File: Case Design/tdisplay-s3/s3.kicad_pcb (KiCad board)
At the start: 2 copper layers, 34 x 109.9 mm, 14 parts, among them SW6 SW_PUSH_6mm_H9.5mm, SW7 SW_PUSH_6mm_H9.5mm, SW8 SW_PUSH_6mm_H9.5mm

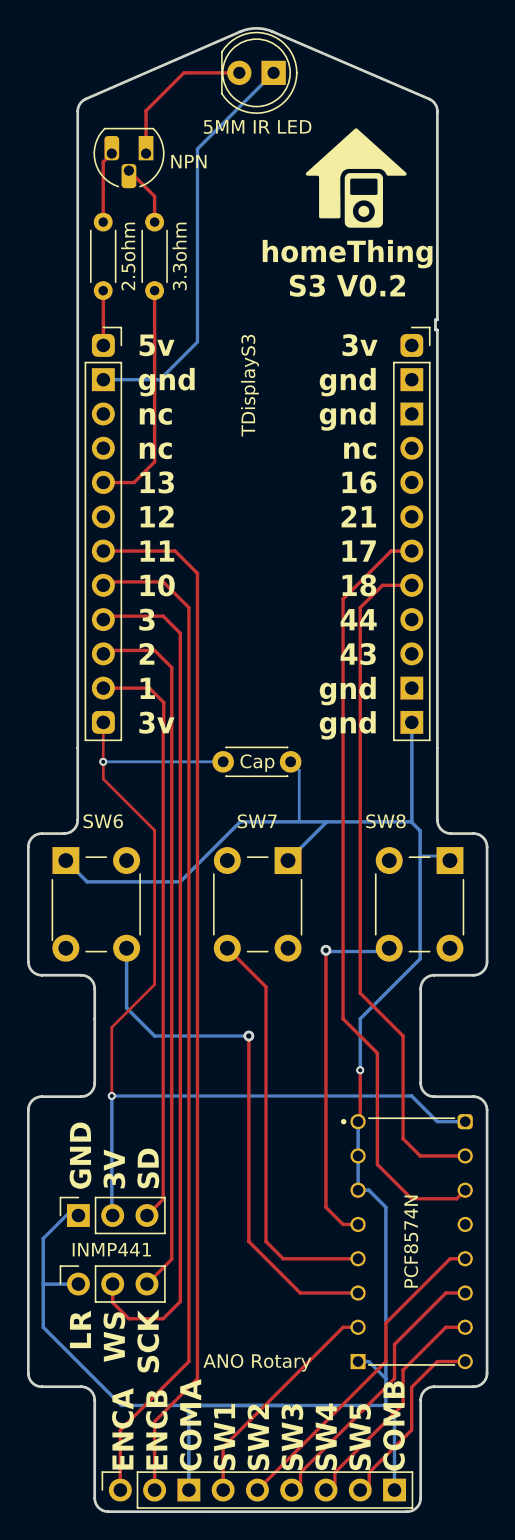
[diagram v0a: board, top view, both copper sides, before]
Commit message: reroute transistor
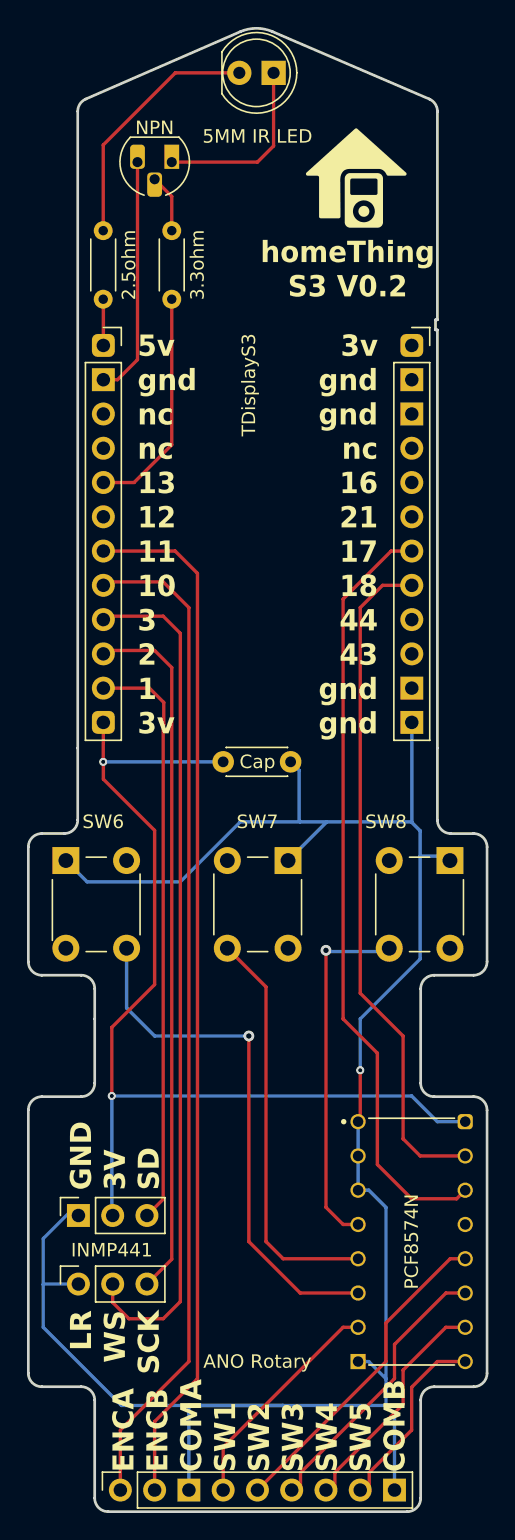
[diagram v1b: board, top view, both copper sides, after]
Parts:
- moved NPN 2.01 mm to (203.8, 52.1)
- moved 3.3ohm 1.42 mm to (203.8, 62.2)
- moved 2.5ohm 0.63 mm to (198.8, 62.2)
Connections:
- 5MM IR LED pad 1: irled -> 5v
- NPN pad 1: irled -> ground2
- NPN pad 3: 5v -> ground2
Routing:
- net 5v: track 9.41 -> 22.1 mm
- net irled: track 33.0 -> 21.4 mm
- net ground2: track 30.4 -> 31.3 mm

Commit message: update ir blaster on pcb
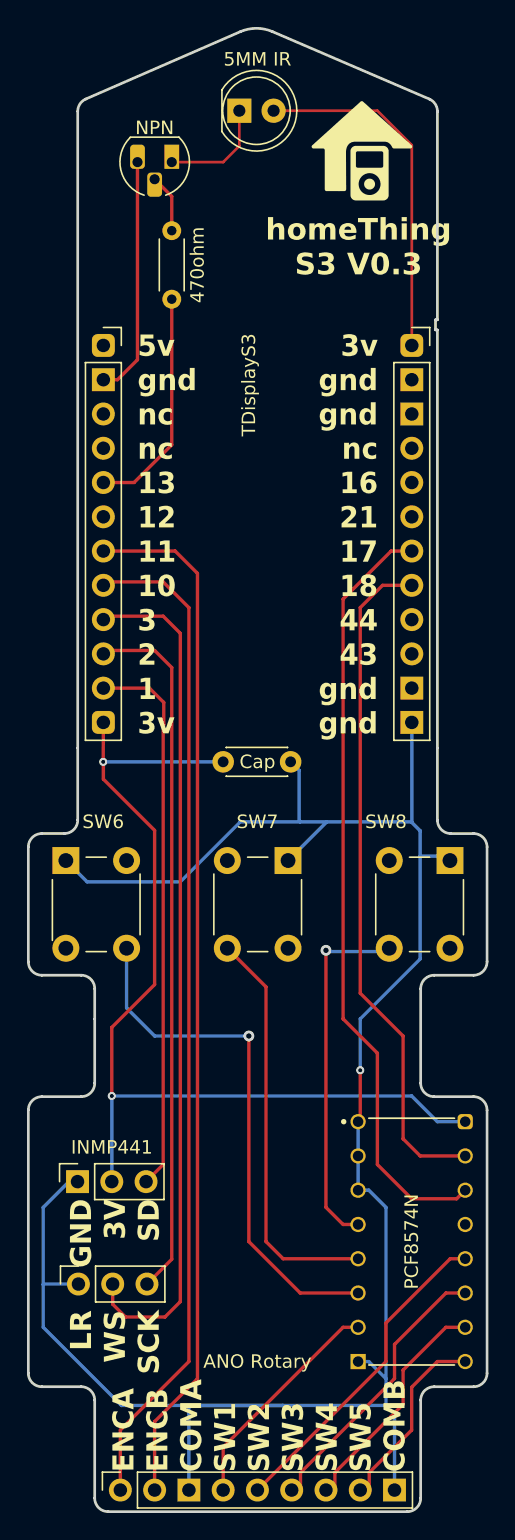
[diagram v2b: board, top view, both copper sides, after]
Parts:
- removed 2.5ohm: R_Axial_DIN0204_L3.6mm_D1.6mm_P5.08mm_Horizontal, Resistor_THT:R_Axial_DIN0204_L3.6mm_D1.6mm_P5.08mm_Horizontal
- 5MM IR: renamed from 5MM IR LED
- moved 5MM IR 2.81 mm to (208.8, 48.3)
- moved INMP441 2.51 mm to (196.8, 127.6)
- renumbered 3.3ohm to 470ohm
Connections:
- 5MM IR pad 1: 5v -> irled
- 5MM IR pad 2: ground2 -> 3v2
- NPN pad 1: ground2 -> irled
- REF** pad 1: (no net) -> 3v2
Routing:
- net 3v2: track 0.00 -> 26.1 mm
- net 5v: track 22.1 -> 0.00 mm
- net ground2: track 31.3 -> 17.8 mm
- net irled: track 21.4 -> 29.5 mm
- net 3v: track 75.3 -> 72.8 mm
- net sd: track 43.5 -> 41.0 mm
- net ground: track 157.8 -> 158.8 mm
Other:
- board text added: "homeThing S3 V0.3"
- board text removed: "homeThing S3 V0.2"

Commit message: pcb updates add 3v + symbol to LED add pcf8574n up symbol make resistor gap larger
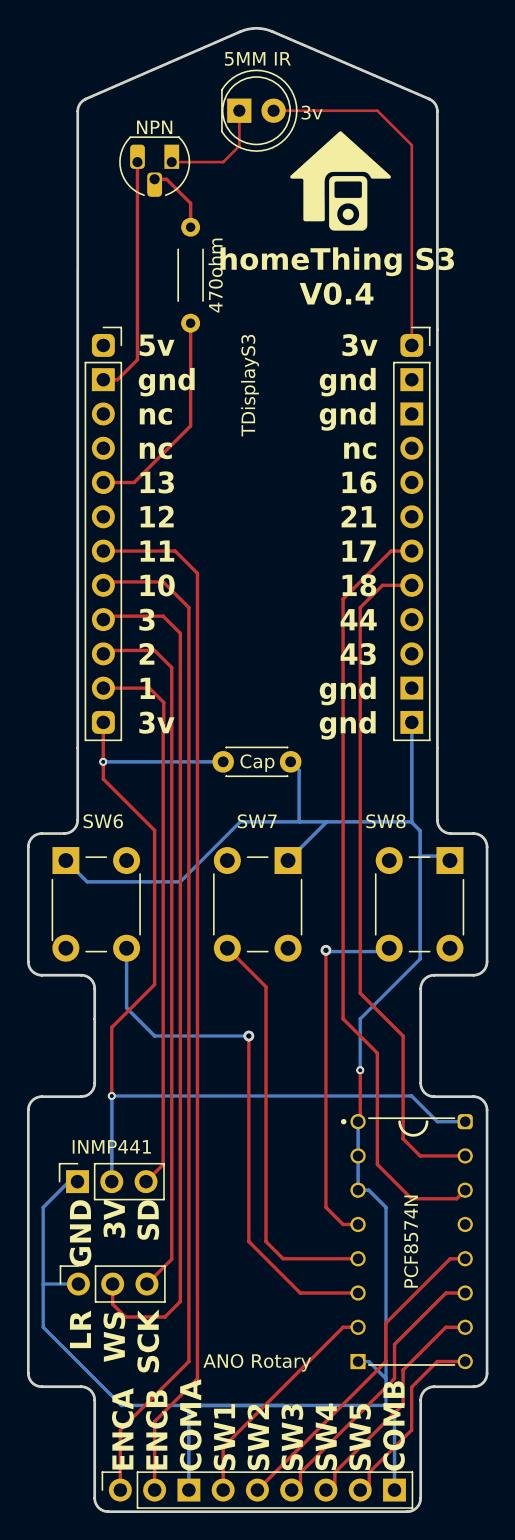
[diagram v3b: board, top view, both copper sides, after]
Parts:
- moved 470ohm 1.59 mm to (205.2, 63.0)
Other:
- outline, holes or cut-outs redrawn
- board text added: "3v"
- board text added: "homeThing S3 V0.4"
- board text removed: "homeThing S3 V0.3"
